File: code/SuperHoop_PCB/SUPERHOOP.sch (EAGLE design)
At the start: 12 parts, among them CON1 Battery_lithium 3.7v (3x), CON2 TOUCH_INPUT, CON3 LED_STRING_OUTPUT, CON4 ADXL335_BBOARD_V2, CON5 ISP-AVR_6P, IC1 MEGA8-P

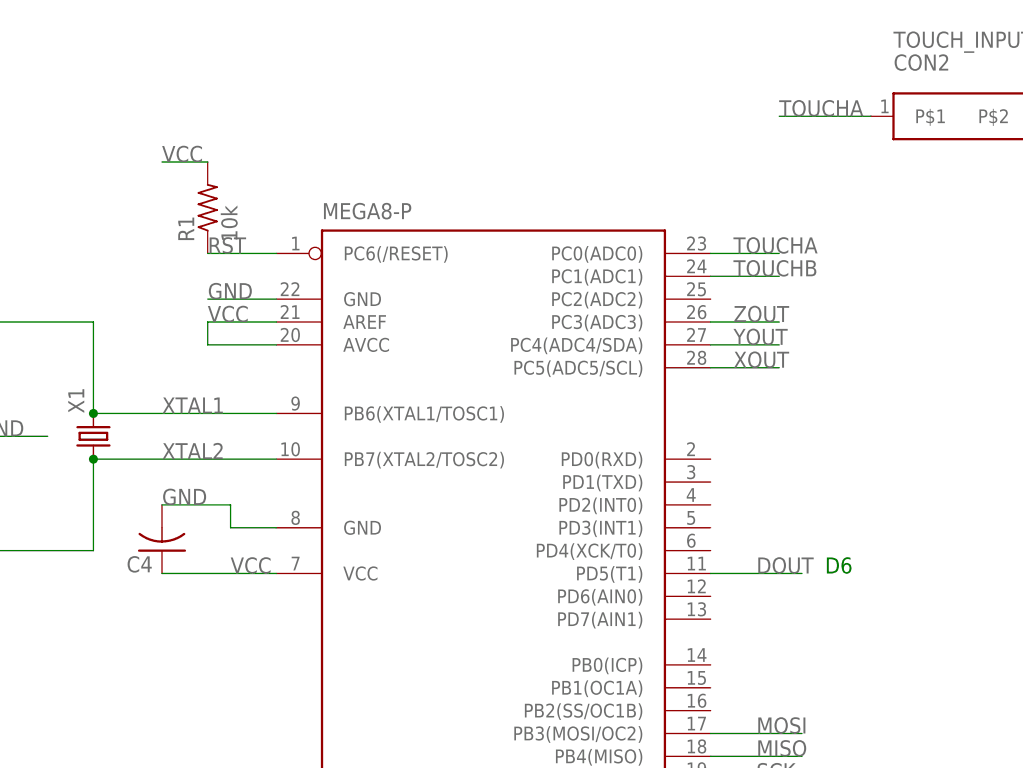
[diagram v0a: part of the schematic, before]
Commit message: Fixed wrong wiring
made the board wiring more readable
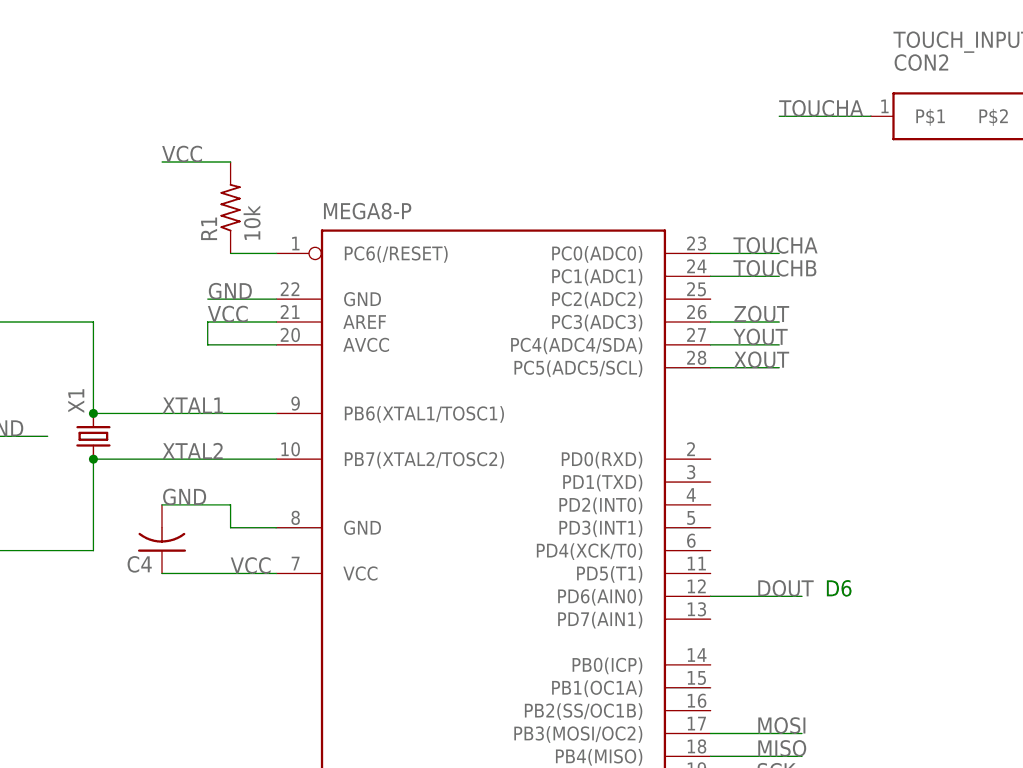
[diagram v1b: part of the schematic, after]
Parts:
- R1: device rcl:R-US_0204/2V -> rcl:R-US_0207/12
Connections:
- new net N$1: IC1.PC6(/RESET), R1.1
- net DOUT: now also IC1.PD6(AIN0); no longer IC1.PD5(T1)
- net RST: no longer IC1.PC6(/RESET), R1.1
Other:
- moved on the sheet: R1
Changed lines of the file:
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@@
 <part name="CON5" library="daneagle_db" deviceset="ISP-AVR" device="_6P"/>
 <part name="X1" library="crystal" deviceset="CRYSTAL" device="HC49S"/>
-<part name="R1" library="rcl" deviceset="R-US_" device="0204/2V" value="10k"/>
+<part name="R1" library="rcl" deviceset="R-US_" device="0207/12" value="10k"/>
 </parts>
 <sheets>
@@
 <text x="233.68" y="106.68" size="1.778" layer="91">XOUT</text>
 <text x="233.68" y="116.84" size="1.778" layer="91">3VO</text>
-<text x="147.32" y="137.16" size="1.778" layer="91">D6</text>
+<text x="147.32" y="134.62" size="1.778" layer="91">D6</text>
 <text x="177.8" y="30.48" size="1.778" layer="91">SUPERHOOP_MAIN_PCB REV --</text>
 </plain>
@@
 <instance part="CON5" gate="G$1" x="154.94" y="76.2"/>
 <instance part="X1" gate="G$1" x="66.04" y="152.4" rot="R90"/>
-<instance part="R1" gate="G$1" x="78.74" y="177.8" rot="R90"/>
+<instance part="R1" gate="G$1" x="81.28" y="177.8" rot="R90"/>
 </instances>
 <busses>
@@
 <segment>
 <pinref part="R1" gate="G$1" pin="2"/>
-<wire x1="73.66" y1="182.88" x2="78.74" y2="182.88" width="0.1524" layer="91"/>
+<wire x1="73.66" y1="182.88" x2="81.28" y2="182.88" width="0.1524" layer="91"/>
 <label x="73.66" y="182.88" size="1.778" layer="95"/>
 </segment>
@@
 </segment>
 <segment>
-<wire x1="144.78" y1="137.16" x2="134.62" y2="137.16" width="0.1524" layer="91"/>
-<label x="139.7" y="137.16" size="1.778" layer="95"/>
-<pinref part="IC1" gate="G$1" pin="PD5(T1)"/>
+<label x="139.7" y="134.62" size="1.778" layer="95"/>
+<pinref part="IC1" gate="G$1" pin="PD6(AIN0)"/>
+<wire x1="144.78" y1="134.62" x2="134.62" y2="134.62" width="0.1524" layer="91"/>
 </segment>
 </net>
@@
 <label x="134.62" y="73.66" size="1.778" layer="95"/>
 </segment>
-<segment>
-<pinref part="IC1" gate="G$1" pin="PC6(/RESET)"/>
-<wire x1="78.74" y1="172.72" x2="86.36" y2="172.72" width="0.1524" layer="91"/>
-<label x="78.74" y="172.72" size="1.778" layer="95"/>
-<pinref part="R1" gate="G$1" pin="1"/>
-</segment>
 </net>
 <net name="MOSI" class="0">
@@
 </segment>
 </net>
+<net name="N$1" class="0">
+<segment>
+<pinref part="R1" gate="G$1" pin="1"/>
+<pinref part="IC1" gate="G$1" pin="PC6(/RESET)"/>
+<wire x1="81.28" y1="172.72" x2="86.36" y2="172.72" width="0.1524" layer="91"/>
+</segment>
+</net>

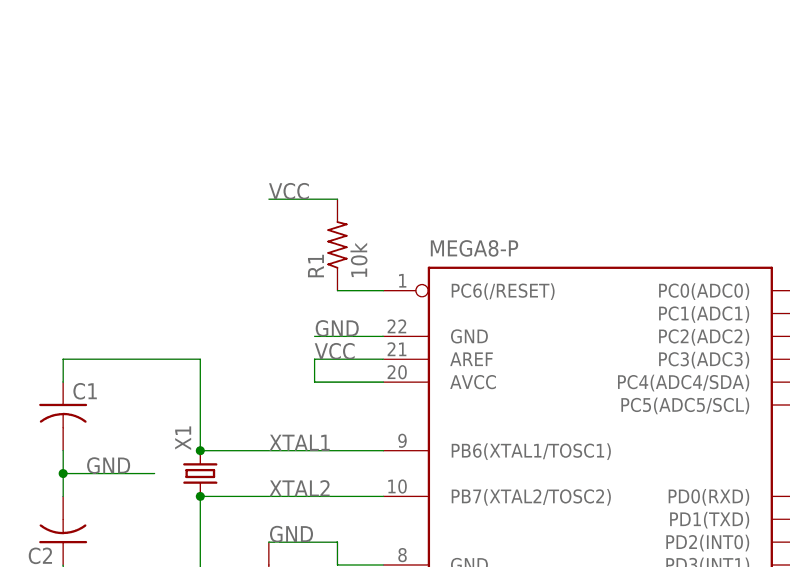
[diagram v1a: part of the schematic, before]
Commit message: Converted patterns to const
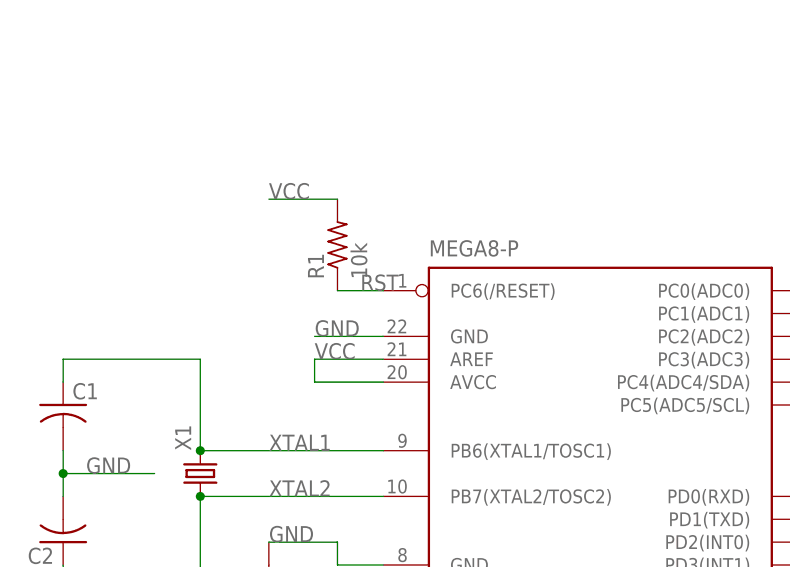
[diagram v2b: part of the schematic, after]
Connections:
- removed net N$1: IC1.PC6(/RESET), R1.1
- net RST: now also IC1.PC6(/RESET), R1.1
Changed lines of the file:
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@@
 <label x="134.62" y="73.66" size="1.778" layer="95"/>
+</segment>
+<segment>
+<pinref part="R1" gate="G$1" pin="1"/>
+<pinref part="IC1" gate="G$1" pin="PC6(/RESET)"/>
+<wire x1="81.28" y1="172.72" x2="86.36" y2="172.72" width="0.1524" layer="91"/>
+<label x="83.82" y="172.72" size="1.778" layer="95"/>
 </segment>
 </net>
@@
 </segment>
 </net>
-<net name="N$1" class="0">
-<segment>
-<pinref part="R1" gate="G$1" pin="1"/>
-<pinref part="IC1" gate="G$1" pin="PC6(/RESET)"/>
-<wire x1="81.28" y1="172.72" x2="86.36" y2="172.72" width="0.1524" layer="91"/>
-</segment>
-</net>
